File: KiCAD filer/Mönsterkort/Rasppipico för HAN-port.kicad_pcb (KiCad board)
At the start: 2 copper layers, 33.8 x 78 mm, 3 parts, among them J1 RJ12

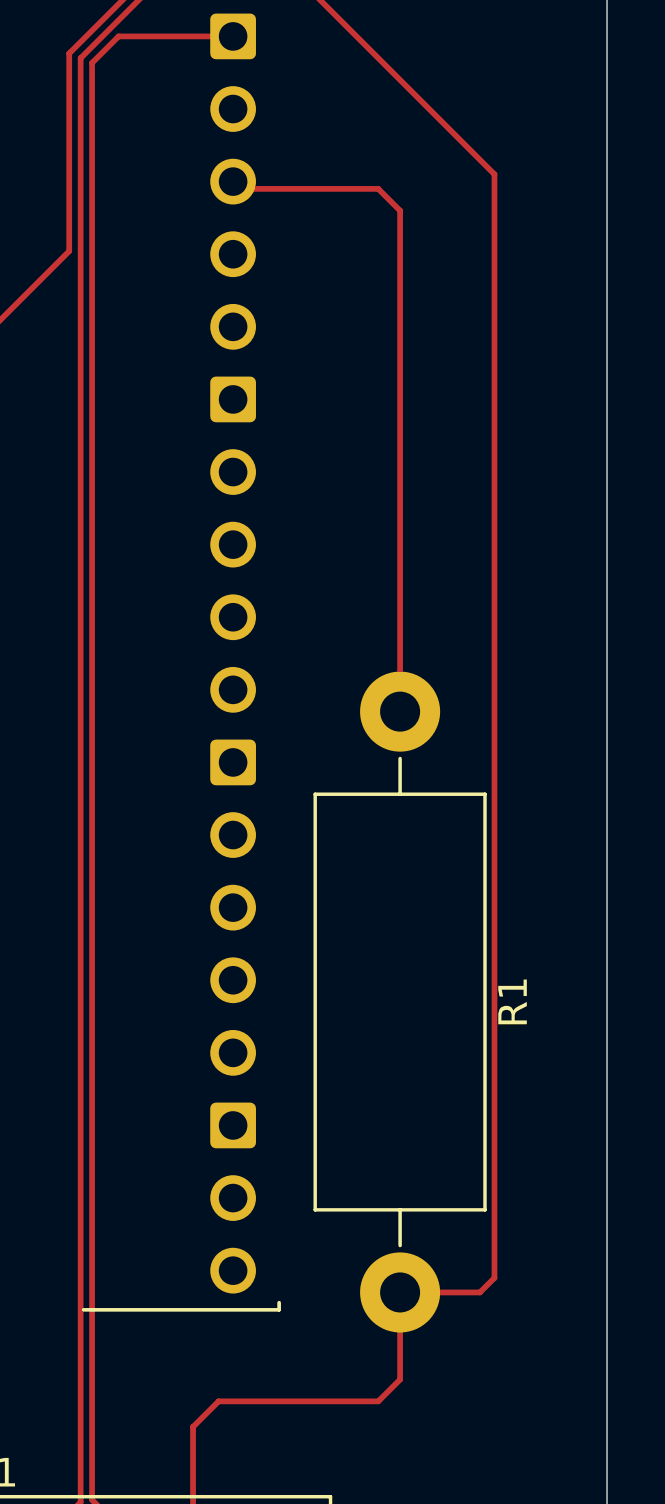
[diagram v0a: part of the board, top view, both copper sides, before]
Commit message: Updaterar filer för PCB.
Fixade storleken på motståndet.
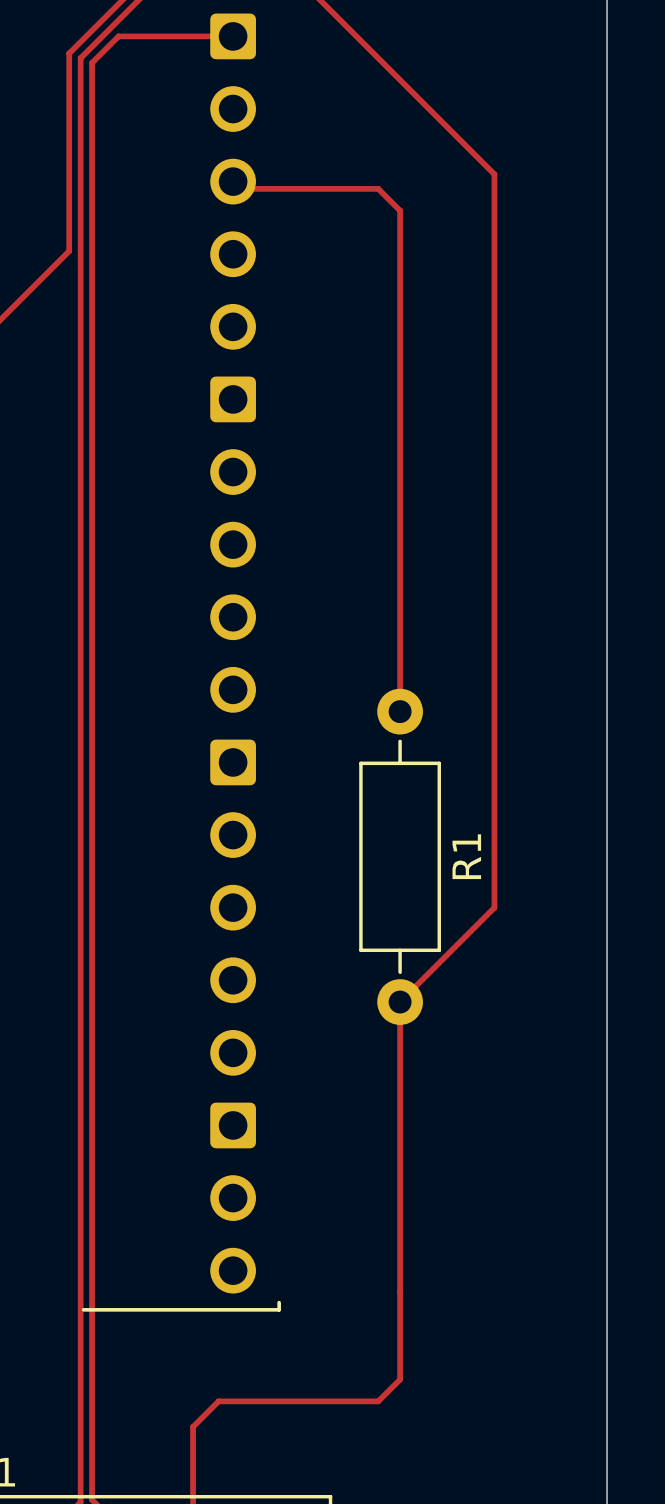
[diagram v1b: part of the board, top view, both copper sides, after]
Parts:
- R1: footprint Resistor_THT:R_Axial_DIN0614_L14.3mm_D5.7mm_P20.32mm_Horizontal -> Resistor_THT:R_Axial_DIN0207_L6.3mm_D2.5mm_P10.16mm_Horizontal
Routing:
- net /Data out: track 97.2 -> 95.6 mm
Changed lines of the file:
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@@
 		)
 	)
-	(footprint "Resistor_THT:R_Axial_DIN0614_L14.3mm_D5.7mm_P20.32mm_Horizontal"
+	(footprint "Resistor_THT:R_Axial_DIN0207_L6.3mm_D2.5mm_P10.16mm_Horizontal"
 		(layer "F.Cu")
 		(at 156.718 84.328 -90)
-		(descr "Resistor, Axial_DIN0614 series, Axial, Horizontal, pin pitch=20.32mm, 1.5W, length*diameter=14.3*5.7mm^2")
-		(tags "Resistor Axial_DIN0614 series Axial Horizontal pin pitch 20.32mm 1.5W length 14.3mm diameter 5.7mm")
+		(descr "Resistor, Axial_DIN0207 series, Axial, Horizontal, pin pitch=10.16mm, 0.25W = 1/4W, length*diameter=6.3*2.5mm^2, http://cdn-reichelt.de/documents/datenblatt/B400/1_4W%23YAG.pdf")
+		(tags "Resistor Axial_DIN0207 series Axial Horizontal pin pitch 10.16mm 0.25W = 1/4W length 6.3mm diameter 2.5mm")
 		(property "Reference" "R1"
-			(at 10.16 -3.97 90)
+			(at 5.08 -2.37 -90)
 			(layer "F.SilkS")
 			(effects
@@
 		)
 		(property "Value" "3k"
-			(at 10.16 3.97 90)
+			(at 5.08 2.37 -90)
 			(layer "F.Fab")
 			(effects
@@
 			)
 		)
-		(property "Footprint" "Resistor_THT:R_Axial_DIN0614_L14.3mm_D5.7mm_P20.32mm_Horizontal"
+		(property "Footprint" "Resistor_THT:R_Axial_DIN0207_L6.3mm_D2.5mm_P10.16mm_Horizontal"
 			(at 0 0 -90)
 			(unlocked yes)
@@
 		(attr through_hole)
 		(fp_line
-			(start 2.89 2.97)
-			(end 17.43 2.97)
+			(start 1.81 1.37)
+			(end 8.35 1.37)
 			(stroke
 				(width 0.12)
@@
 		)
 		(fp_line
-			(start 17.43 2.97)
-			(end 17.43 -2.97)
+			(start 8.35 1.37)
+			(end 8.35 -1.37)
 			(stroke
 				(width 0.12)
@@
 		)
 		(fp_line
-			(start 1.64 0)
-			(end 2.89 0)
+			(start 1.04 0)
+			(end 1.81 0)
 			(stroke
 				(width 0.12)
@@
 		)
 		(fp_line
-			(start 18.68 0)
-			(end 17.43 0)
+			(start 9.12 0)
+			(end 8.35 0)
 			(stroke
 				(width 0.12)
@@
 		)
 		(fp_line
-			(start 2.89 -2.97)
-			(end 2.89 2.97)
+			(start 1.81 -1.37)
+			(end 1.81 1.37)
 			(stroke
 				(width 0.12)
@@
 		)
 		(fp_line
-			(start 17.43 -2.97)
-			(end 2.89 -2.97)
+			(start 8.35 -1.37)
+			(end 1.81 -1.37)
 			(stroke
 				(width 0.12)
@@
 		)
 		(fp_line
-			(start -1.65 3.1)
-			(end 21.97 3.1)
+			(start -1.05 1.5)
+			(end 11.21 1.5)
 			(stroke
 				(width 0.05)
@@
 		)
 		(fp_line
-			(start 21.97 3.1)
-			(end 21.97 -3.1)
+			(start 11.21 1.5)
+			(end 11.21 -1.5)
 			(stroke
 				(width 0.05)
@@
 		)
 		(fp_line
-			(start -1.65 -3.1)
-			(end -1.65 3.1)
+			(start -1.05 -1.5)
+			(end -1.05 1.5)
 			(stroke
 				(width 0.05)
@@
 		)
 		(fp_line
-			(start 21.97 -3.1)
-			(end -1.65 -3.1)
+			(start 11.21 -1.5)
+			(end -1.05 -1.5)
 			(stroke
 				(width 0.05)
@@
 		)
 		(fp_line
-			(start 3.01 2.85)
-			(end 17.31 2.85)
+			(start 1.93 1.25)
+			(end 8.23 1.25)
 			(stroke
 				(width 0.1)
@@
 		)
 		(fp_line
-			(start 17.31 2.85)
-			(end 17.31 -2.85)
+			(start 8.23 1.25)
+			(end 8.23 -1.25)
 			(stroke
 				(width 0.1)
@@
 		(fp_line
 			(start 0 0)
-			(end 3.01 0)
+			(end 1.93 0)
 			(stroke
 				(width 0.1)
@@
 		)
 		(fp_line
-			(start 20.32 0)
-			(end 17.31 0)
+			(start 10.16 0)
+			(end 8.23 0)
 			(stroke
 				(width 0.1)
@@
 		)
 		(fp_line
-			(start 3.01 -2.85)
-			(end 3.01 2.85)
+			(start 1.93 -1.25)
+			(end 1.93 1.25)
 			(stroke
 				(width 0.1)
@@
 		)
 		(fp_line
-			(start 17.31 -2.85)
-			(end 3.01 -2.85)
+			(start 8.23 -1.25)
+			(end 1.93 -1.25)
 			(stroke
 				(width 0.1)
@@
 		)
 		(fp_text user "${REFERENCE}"
-			(at 10.16 0 90)
+			(at 5.08 0 -90)
 			(layer "F.Fab")
 			(effects
@@
 		(pad "1" thru_hole circle
 			(at 0 0 270)
-			(size 2.8 2.8)
-			(drill 1.4)
+			(size 1.6 1.6)
+			(drill 0.8)
 			(layers "*.Cu" "*.Mask")
 			(remove_unused_layers no)
@@
 		)
 		(pad "2" thru_hole oval
-			(at 20.32 0 270)
-			(size 2.8 2.8)
-			(drill 1.4)
+			(at 10.16 0 270)
+			(size 1.6 1.6)
+			(drill 0.8)
 			(layers "*.Cu" "*.Mask")
 			(remove_unused_layers no)
@@
 			(pintype "passive")
 		)
-		(model "${KICAD8_3DMODEL_DIR}/Resistor_THT.3dshapes/R_Axial_DIN0614_L14.3mm_D5.7mm_P20.32mm_Horizontal.wrl"
+		(model "${KICAD8_3DMODEL_DIR}/Resistor_THT.3dshapes/R_Axial_DIN0207_L6.3mm_D2.5mm_P10.16mm_Horizontal.wrl"
 			(offset
 				(xyz 0 0 0)
@@
 	)
 	(segment
+		(start 160.02 65.532)
+		(end 151.384 56.896)
+		(width 0.2)
+		(layer "F.Cu")
+		(net 2)
+	)
+	(segment
+		(start 145.142 61.302314)
+		(end 145.142 68.218)
+		(width 0.2)
+		(layer "F.Cu")
+		(net 2)
+	)
+	(segment
+		(start 156.718 107.696)
+		(end 156.718 104.648)
+		(width 0.2)
+		(layer "F.Cu")
+		(net 2)
+	)
+	(segment
+		(start 155.956 108.458)
+		(end 156.718 107.696)
+		(width 0.2)
+		(layer "F.Cu")
+		(net 2)
+	)
+	(segment
+		(start 149.474 113.134)
+		(end 149.474 109.352)
+		(width 0.2)
+		(layer "F.Cu")
+		(net 2)
+	)
+	(segment
+		(start 151.384 56.896)
+		(end 149.548314 56.896)
+		(width 0.2)
+		(layer "F.Cu")
+		(net 2)
+	)
+	(segment
 		(start 149.548314 56.896)
 		(end 145.142 61.302314)
@@
 	)
 	(segment
-		(start 156.718 107.696)
-		(end 156.718 104.648)
+		(start 150.368 108.458)
+		(end 155.956 108.458)
+		(width 0.2)
+		(layer "F.Cu")
+		(net 2)
+	)
+	(segment
+		(start 149.474 109.352)
+		(end 150.368 108.458)
+		(width 0.2)
+		(layer "F.Cu")
+		(net 2)
+	)
+	(segment
+		(start 160.02 91.186)
+		(end 160.02 65.532)
 		(width 0.2)
 		(layer "F.Cu")
@@
 	)
 	(segment
-		(start 155.956 108.458)
-		(end 156.718 107.696)
-		(width 0.2)
-		(layer "F.Cu")
-		(net 2)
-	)
-	(segment
-		(start 151.384 56.896)
-		(end 149.548314 56.896)
-		(width 0.2)
-		(layer "F.Cu")
-		(net 2)
-	)
-	(segment
-		(start 156.718 104.648)
-		(end 159.512 104.648)
-		(width 0.2)
-		(layer "F.Cu")
-		(net 2)
-	)
-	(segment
-		(start 149.474 113.134)
-		(end 149.474 109.352)
-		(width 0.2)
-		(layer "F.Cu")
-		(net 2)
-	)
-	(segment
-		(start 160.02 104.14)
-		(end 160.02 65.532)
-		(width 0.2)
-		(layer "F.Cu")
-		(net 2)
-	)
-	(segment
-		(start 145.142 61.302314)
-		(end 145.142 68.218)
-		(width 0.2)
-		(layer "F.Cu")
-		(net 2)
-	)
-	(segment
-		(start 160.02 65.532)
-		(end 151.384 56.896)
-		(width 0.2)
-		(layer "F.Cu")
-		(net 2)
-	)
-	(segment
-		(start 150.368 108.458)
-		(end 155.956 108.458)
-		(width 0.2)
-		(layer "F.Cu")
-		(net 2)
-	)
-	(segment
-		(start 149.474 109.352)
-		(end 150.368 108.458)
-		(width 0.2)
-		(layer "F.Cu")
-		(net 2)
-	)
-	(segment
 		(start 145.142 68.218)
 		(end 142.494 70.866)
@@
 	)
 	(segment
-		(start 159.512 104.648)
-		(end 160.02 104.14)
-		(width 0.2)
-		(layer "F.Cu")
+		(start 156.718 104.648)
+		(end 156.718 94.488)
+		(width 0.2)
+		(layer "F.Cu")
+		(net 2)
+	)
+	(segment
+		(start 156.718 94.488)
+		(end 160.02 91.186)
+		(width 0.2)
+		(layer "F.Cu")

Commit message: Uppdatering av filer och la till stl filer
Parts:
- moved J1 38.9 mm to (112.9, 90.4), turned to -90 degrees
- moved R1 22.5 mm to (143.7, 102.7), turned to 180 degrees
- moved A1 10.3 mm to (148.2, 88.0), turned to -90 degrees
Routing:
- net /Data out: track 95.6 -> 97.6 mm
- net VCC: track 61.6 -> 63.5 mm
- net GND: track 62.4 -> 64.1 mm
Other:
- board size 33.8 x 78 mm -> 80 x 35 mm
